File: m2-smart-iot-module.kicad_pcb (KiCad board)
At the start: 4 copper layers, 80.2 x 22.1 mm, 165 parts, among them J1 MM8130-2600RA2, J2 2X05, J3 M.2-M+B-Pins, Q1 BSS123, SW1 PTS840_GK_SMTR_LFS, SW2 PTS840_GK_SMTR_LFS, U1 UPD720202, U10 MIC2877-5.0YFT-TR, U2 SST25VF512A, U3 CoralAccelerator, U4 NRF52840, U5 AP2120N-1.8TRG1, U6 AP22652W6-7, U7 TLV803EF29DBZR, U8 BME280, U9 NCP1599MNTWG, Y1 NX3225SA-24M, Y2 ABM11W-101-32.0000MHZ-T3, Y3 ABS06-32.768KHZ-9-1-T

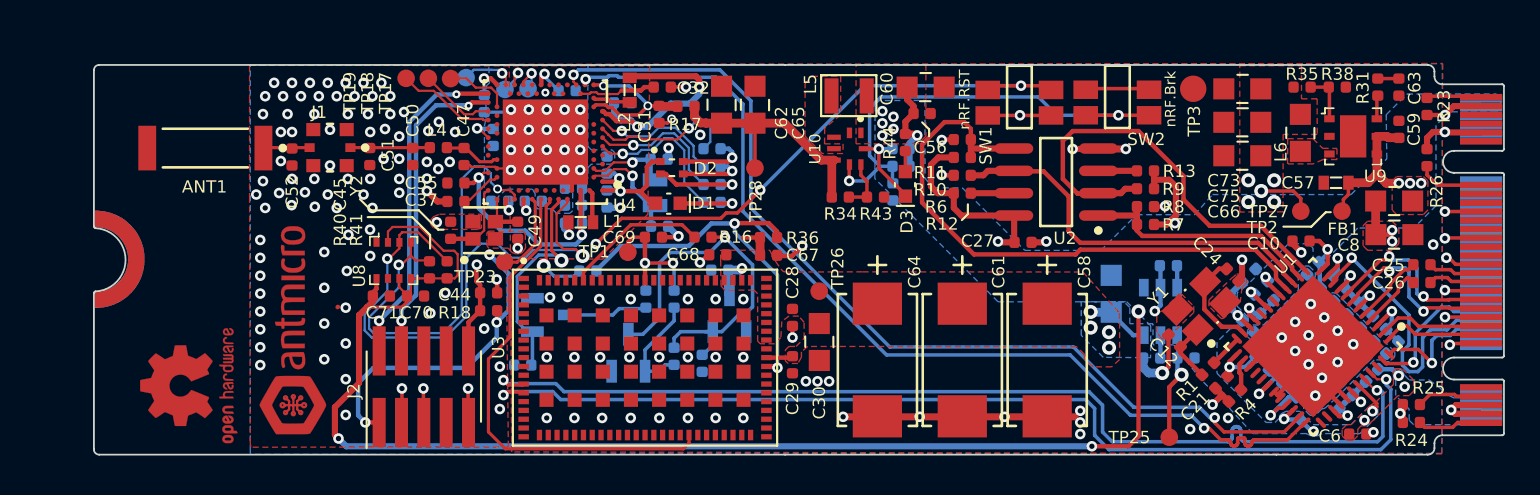
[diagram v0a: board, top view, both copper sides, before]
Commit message: Rearrangement of JTAG connector and U8 sensor
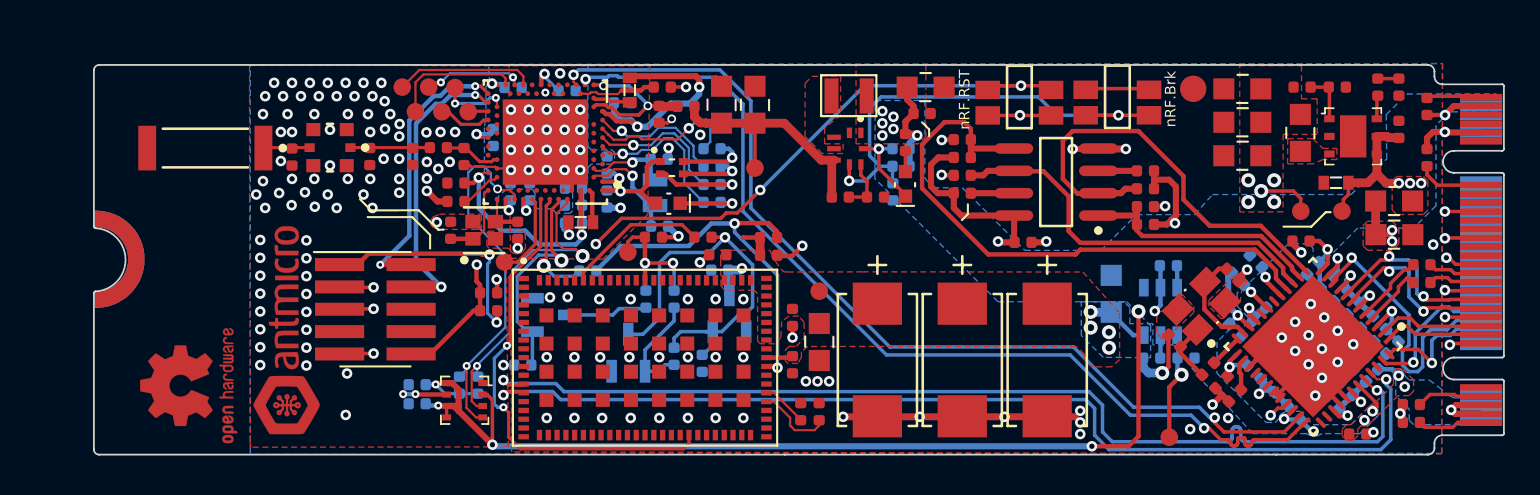
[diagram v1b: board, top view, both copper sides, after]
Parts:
- added R45: R_0R_0402, antmicro-footprints:0402-res, F.Cu at (155.9, 111.2)
- added R46: R_0R_0402, antmicro-footprints:0402-res, F.Cu at (154.9, 111.2)
- C70, C71, R40, R41: moved to B.Cu
- TP11, TP12, TP16: moved to F.Cu
- moved U8 8.91 mm to (135.8, 110.5), turned to 270 degrees
- moved TP11 7.15 mm to (132.2, 92.8)
- moved R41 6.78 mm to (136.6, 109.6)
- moved R40 6.77 mm to (135.5, 109.6)
- moved C70 6.13 mm to (133.1, 110.7), turned to 0 degrees
- moved C71 5.43 mm to (133.1, 109.6), turned to 180 degrees
- moved J2 4.84 mm to (131.0, 105.3), turned to 270 degrees
- moved TP12 4.34 mm to (133.8, 92.8)
- moved TP16 3.53 mm to (133.0, 94.2)
- moved TP18 2.96 mm to (136.0, 94.2)
- moved TP19 2.78 mm to (134.5, 94.2)
- moved C41 1.88 mm to (138.6, 92.7), turned to 0 degrees
- moved R5 0.84 mm to (180.8, 102.6)
- moved C39 0.81 mm to (138.4, 98.7), turned to 90 degrees
- moved R3 0.80 mm to (179.8, 103.6)
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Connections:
- net Net-(C54-Pad1) renamed /CoralAccelerator/1V8_CORAL
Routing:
- net 3V3: track 123.5 -> 106.1 mm, vias 22 -> 24
- net /nRF52840/SDA: track 31.6 -> 18.9 mm
- net Net-(TP11-Pad1): track 1.80 -> 7.93 mm, vias 1 -> 0
- net /nRF52840/VDD: track 47.5 -> 42.6 mm, vias 9 -> 8
- net Net-(R45-Pad1): track 0.00 -> 4.34 mm
- net /nRF52840/SCL: track 25.2 -> 21.1 mm
- net Net-(TP12-Pad1): track 2.18 -> 5.68 mm, vias 1 -> 2
- net Net-(TP18-Pad1): track 4.32 -> 1.17 mm
- net /nRF52840/SWDIO: track 18.9 -> 16.1 mm
- net Net-(R46-Pad1): track 0.00 -> 2.62 mm
- net Net-(TP19-Pad1): track 5.65 -> 3.08 mm
- net Net-(TP16-Pad1): track 4.98 -> 7.35 mm, vias 1 -> 0
- net /nRF52840/~RESET: track 58.2 -> 60.4 mm
- net /nRF52840/SWCLK: track 17.8 -> 16.5 mm
- net GND: track 88.3 -> 89.5 mm, vias 189 -> 185
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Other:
- board text added: "PCIe radio module rev 1.1.0 03/2022"
- board text removed: "ePCI radio module rev 1.1.0 03/2022"

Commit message: Moved antenna out of GND plane
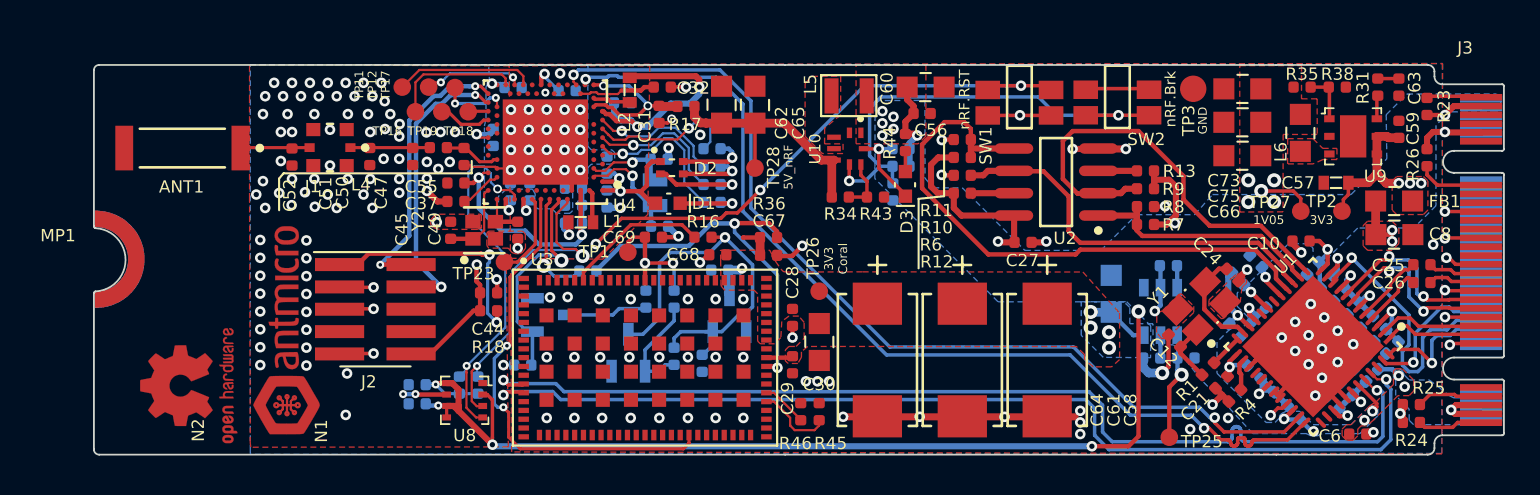
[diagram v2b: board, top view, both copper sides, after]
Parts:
- moved ANT1 1.31 mm to (119.8, 96.2)
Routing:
- net Net-(ANT1-Pad1): track 2.70 -> 3.94 mm
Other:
- board text added: "1V05"
- board text added: "3V3"
- board text added: "3V3 Coral"
- board text added: "5V_nRF"
- board text added: "GND"

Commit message: Updated width and gap of USB and PCIe lanes to correct impedance
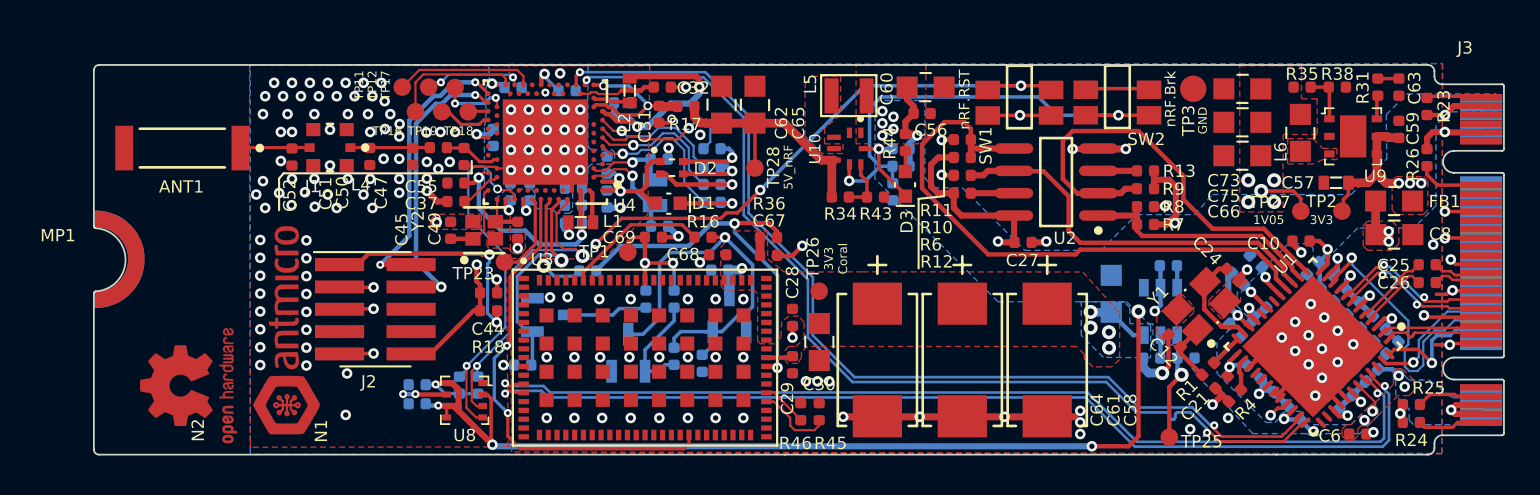
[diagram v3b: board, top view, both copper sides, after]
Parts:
- moved C25 0.30 mm to (190.5, 102.8)
- moved C26 0.30 mm to (190.5, 103.8)
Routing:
- net CORAL_USB_P: track 59.2 -> 56.6 mm
- net GND: track 89.5 -> 91.9 mm
- net PETX_N: track 11.6 -> 9.44 mm
- net PETX_P: track 11.4 -> 9.40 mm
- net CORAL_USB_N: track 58.8 -> 57.3 mm
- net Radio_USB_P: track 54.6 -> 56.1 mm
- net Radio_USB_N: track 55.1 -> 56.1 mm
- net 3V3_CORAL: track 9.35 -> 8.38 mm
- net /PCIe-USB-Bridge/AVDD: track 26.2 -> 25.3 mm
- net 1V05: track 83.6 -> 83.0 mm
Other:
- net class Diff_100 added: clearance 0.125, trace_width 0.25, via_dia 0.46, via_drill 0.2
- net class Diff_90: clearance 0.127 -> 0.125; trace_width 0.28 -> 0.25; via_dia 0.6 -> 0.46; via_drill 0.3 -> 0.2

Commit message: Added stackup table to PCB
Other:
- board text added: "0.018 mm"
- board text added: "0.02 mm"
- board text added: "0.035 mm"
- board text added: "0.12 mm"
- board text added: "0.51 mm"
- board text added: "1"
- board text added: "2"
- board text added: "3"
- board text added: "3.5"
- board text added: "4"
- board text added: "4.2"
- board text added: "5"
- board text added: "6"
- board text added: "7"
- board text added: "8"
- board text added: "9"
- board text added: "Bottom Layer"
- board text added: "Bottom Solder"
- board text added: "Constant"
- board text added: "Copper"
- board text added: "Dielectric 1"
- board text added: "Dielectric 2"
- board text added: "Dielectric 3"
- board text added: "FR-4"
- board text added: "Gold plating (ENIG, selective)"
- board text added: "Layer"
- board text added: "Material"
- board text added: "Name"
- board text added: "Power Plane 1"
- board text added: "Power Plane 2"
- board text added: "Prepreg"
- board text added: "Recommended PCB finish:"
- board text added: "Recommended PCB stackup"
- board text added: "Silkscreen: white"
- board text added: "Solder Resist"
- board text added: "Solder mask: matt black"
- board text added: "Suggested prepreg material is ISOLA PR2116"
- board text added: "The design includes high speed signaling"
- board text added: "Thickness"
- board text added: "Top Layer"
- board text added: "Top Solder"

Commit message: Added 3d models of BME280 and 1V05 DCDC
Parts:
- R45, R46: footprint antmicro-footprints:0402-res -> m2-smart-iot-module-footprints:0402-res
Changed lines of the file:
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@@
     (add_net Radio_USB_P)
+  )
+  (module m2-smart-iot-module-footprints:Pressure_Sensor_LGA-8_2.5x2.5mm_BME280 (layer F.Cu)
+    (at 135.7975 110.5 270)
+    (attr smd)
+    (fp_text reference U8 (at 2 -0.0025) (layer F.SilkS)
+      (effects (font (size 0.7 0.7) (thickness 0.15)))
+    )
+    (fp_text value BME280 (at 0 2.47 90) (layer F.Fab) hide
+      (effects (font (size 1 1) (thickness 0.15)))
+    )
+    (fp_line (start 1.5 1.5) (end -1.5 1.5) (layer F.CrtYd) (width 0.05))
+    (fp_line (start -1.5 -1.5) (end -1.5 1.5) (layer F.CrtYd) (width 0.05))
+    (fp_line (start 1.5 -1.5) (end -1.5 -1.5) (layer F.CrtYd) (width 0.05))
+    (fp_line (start 1.5 -1.5) (end 1.5 1.5) (layer F.CrtYd) (width 0.05))
+    (fp_line (start 1.35 1.35) (end 1.35 0.85) (layer F.SilkS) (width 0.1))
+    (fp_line (start 1.35 1.35) (end 0.85 1.35) (layer F.SilkS) (width 0.1))
+    (fp_line (start -1.35 1.35) (end -1.35 0.85) (layer F.SilkS) (width 0.1))
+    (fp_line (start -1.35 1.35) (end -0.85 1.35) (layer F.SilkS) (width 0.1))
+    (fp_line (start -0.85 -1.35) (end -0.85 -1.55) (layer F.SilkS) (width 0.1))
+    (fp_line (start -1.35 -1.35) (end -1.35 -0.85) (layer F.SilkS) (width 0.1))
+    (fp_line (start -1.35 -1.35) (end -0.85 -1.35) (layer F.SilkS) (width 0.1))
+    (fp_line (start 1.35 -1.35) (end 1.35 -0.975) (layer F.SilkS) (width 0.1))
+    (fp_line (start 1.35 -1.35) (end 0.975 -1.35) (layer F.SilkS) (width 0.1))
+    (fp_text user %R (at 0 0 90) (layer F.Fab)
+      (effects (font (size 0.7 0.7) (thickness 0.05)))
+    )
+    (fp_line (start 1.25 -1.25) (end 1.25 1.25) (layer F.Fab) (width 0.1))
+    (fp_line (start 1.25 1.25) (end -1.25 1.25) (layer F.Fab) (width 0.1))
+    (fp_line (start -1.25 1.25) (end -1.25 -1.25) (layer F.Fab) (width 0.1))
+    (fp_line (start -1.25 -1.25) (end 1.25 -1.25) (layer F.Fab) (width 0.1))
+    (pad 1 smd rect (at -0.975 -1.025 270) (size 0.35 0.5) (layers F.Cu F.Paste F.Mask)
+      (net 1 GND))
+    (pad 2 smd rect (at -0.325 -1.025 270) (size 0.35 0.5) (layers F.Cu F.Paste F.Mask)
+      (net 2 3V3))
+    (pad 3 smd rect (at 0.325 -1.025 270) (size 0.35 0.5) (layers F.Cu F.Paste F.Mask)
+      (net 146 /nRF52840/SDA))
+    (pad 4 smd rect (at 0.975 -1.025 270) (size 0.35 0.5) (layers F.Cu F.Paste F.Mask)
+      (net 147 /nRF52840/SCL))
+    (pad 5 smd rect (at 0.975 1.024999 270) (size 0.35 0.5) (layers F.Cu F.Paste F.Mask)
+      (net 2 3V3))
+    (pad 6 smd rect (at 0.325 1.024999 270) (size 0.35 0.5) (layers F.Cu F.Paste F.Mask)
+      (net 2 3V3))
+    (pad 7 smd rect (at -0.325 1.024999 270) (size 0.35 0.5) (layers F.Cu F.Paste F.Mask)
+      (net 1 GND))
+    (pad 8 smd rect (at -0.975 1.024999 270) (size 0.35 0.5) (layers F.Cu F.Paste F.Mask)
+      (net 2 3V3))
+    (model ${KIPRJMOD}/lib/3d-models/BME280.STEP
+      (at (xyz 0 0 0))
+      (scale (xyz 1 1 1))
+      (rotate (xyz -90 0 180))
+    )
   )
   (module m2-smart-iot-module-footprints:ARM_SWD (layer F.Cu)
@@
     )
   )
-  (module antmicro-footprints:0402-res (layer F.Cu)
+  (module m2-smart-iot-module-footprints:0402-res (layer F.Cu)
     (at 154.9 111.15 90)
     (descr "Resistor SMD 0402 (1005 Metric), square (rectangular) end terminal, IPC_7351 nominal, (Body size source: http://www.tortai-tech.com/upload/download/2011102023233369053.pdf), generated with kicad-footprint-generator")
@@
     (pad 1 smd roundrect (at -0.485 0 90) (size 0.59 0.64) (layers F.Cu F.Paste F.Mask) (roundrect_rratio 0.25)
       (net 178 "Net-(R46-Pad1)"))
-    (model ${ANT3DMDL}/0402-res.step
+    (model ${KIPRJMOD}/lib/3d-models/0402-res.step
       (offset (xyz 0 0 -0.01))
       (scale (xyz 1 1 1))
@@
     )
   )
-  (module antmicro-footprints:0402-res (layer F.Cu)
+  (module m2-smart-iot-module-footprints:0402-res (layer F.Cu)
     (at 155.95 111.15 90)
     (descr "Resistor SMD 0402 (1005 Metric), square (rectangular) end terminal, IPC_7351 nominal, (Body size source: http://www.tortai-tech.com/upload/download/2011102023233369053.pdf), generated with kicad-footprint-generator")
@@
     (pad 1 smd roundrect (at -0.485 0 90) (size 0.59 0.64) (layers F.Cu F.Paste F.Mask) (roundrect_rratio 0.25)
       (net 177 "Net-(R45-Pad1)"))
-    (model ${ANT3DMDL}/0402-res.step
+    (model ${KIPRJMOD}/lib/3d-models/0402-res.step
       (offset (xyz 0 0 -0.01))
       (scale (xyz 1 1 1))
@@
     )
   )
-  (module m2-smart-iot-module-footprints:Pressure_Sensor_LGA-8_2.5x2.5mm_BME280 (layer F.Cu)
-    (at 135.7975 110.5 270)
-    (attr smd)
-    (fp_text reference U8 (at 2 -0.0025) (layer F.SilkS)
-      (effects (font (size 0.7 0.7) (thickness 0.15)))
-    )
-    (fp_text value BME280 (at 0 2.47 90) (layer F.Fab) hide
-      (effects (font (size 1 1) (thickness 0.15)))
-    )
-    (fp_line (start 1.5 1.5) (end -1.5 1.5) (layer F.CrtYd) (width 0.05))
-    (fp_line (start -1.5 -1.5) (end -1.5 1.5) (layer F.CrtYd) (width 0.05))
-    (fp_line (start 1.5 -1.5) (end -1.5 -1.5) (layer F.CrtYd) (width 0.05))
-    (fp_line (start 1.5 -1.5) (end 1.5 1.5) (layer F.CrtYd) (width 0.05))
-    (fp_line (start 1.35 1.35) (end 1.35 0.85) (layer F.SilkS) (width 0.1))
-    (fp_line (start 1.35 1.35) (end 0.85 1.35) (layer F.SilkS) (width 0.1))
-    (fp_line (start -1.35 1.35) (end -1.35 0.85) (layer F.SilkS) (width 0.1))
-    (fp_line (start -1.35 1.35) (end -0.85 1.35) (layer F.SilkS) (width 0.1))
-    (fp_line (start -0.85 -1.35) (end -0.85 -1.55) (layer F.SilkS) (width 0.1))
-    (fp_line (start -1.35 -1.35) (end -1.35 -0.85) (layer F.SilkS) (width 0.1))
-    (fp_line (start -1.35 -1.35) (end -0.85 -1.35) (layer F.SilkS) (width 0.1))
-    (fp_line (start 1.35 -1.35) (end 1.35 -0.975) (layer F.SilkS) (width 0.1))
-    (fp_line (start 1.35 -1.35) (end 0.975 -1.35) (layer F.SilkS) (width 0.1))
-    (fp_line (start 1.25 -1.25) (end 1.25 1.25) (layer F.Fab) (width 0.1))
-    (fp_line (start 1.25 1.25) (end -1.25 1.25) (layer F.Fab) (width 0.1))
-    (fp_line (start -1.25 1.25) (end -1.25 -1.25) (layer F.Fab) (width 0.1))
-    (fp_line (start -1.25 -1.25) (end 1.25 -1.25) (layer F.Fab) (width 0.1))
-    (fp_text user %R (at 0 0 90) (layer F.Fab)
-      (effects (font (size 0.7 0.7) (thickness 0.05)))
-    )
-    (pad 8 smd rect (at -0.975 1.024999 270) (size 0.35 0.5) (layers F.Cu F.Paste F.Mask)
-      (net 2 3V3))
-    (pad 7 smd rect (at -0.325 1.024999 270) (size 0.35 0.5) (layers F.Cu F.Paste F.Mask)
-      (net 1 GND))
-    (pad 6 smd rect (at 0.325 1.024999 270) (size 0.35 0.5) (layers F.Cu F.Paste F.Mask)
-      (net 2 3V3))
-    (pad 5 smd rect (at 0.975 1.024999 270) (size 0.35 0.5) (layers F.Cu F.Paste F.Mask)
-      (net 2 3V3))
-    (pad 4 smd rect (at 0.975 -1.025 270) (size 0.35 0.5) (layers F.Cu F.Paste F.Mask)
-      (net 147 /nRF52840/SCL))
-    (pad 3 smd rect (at 0.325 -1.025 270) (size 0.35 0.5) (layers F.Cu F.Paste F.Mask)
-      (net 146 /nRF52840/SDA))
-    (pad 2 smd rect (at -0.325 -1.025 270) (size 0.35 0.5) (layers F.Cu F.Paste F.Mask)
-      (net 2 3V3))
-    (pad 1 smd rect (at -0.975 -1.025 270) (size 0.35 0.5) (layers F.Cu F.Paste F.Mask)
-      (net 1 GND))
-  )
   (module m2-smart-iot-module-footprints:Nordic_Semiconductor-NRF52840-QIAA-R-0-0-MFG (layer F.Cu)

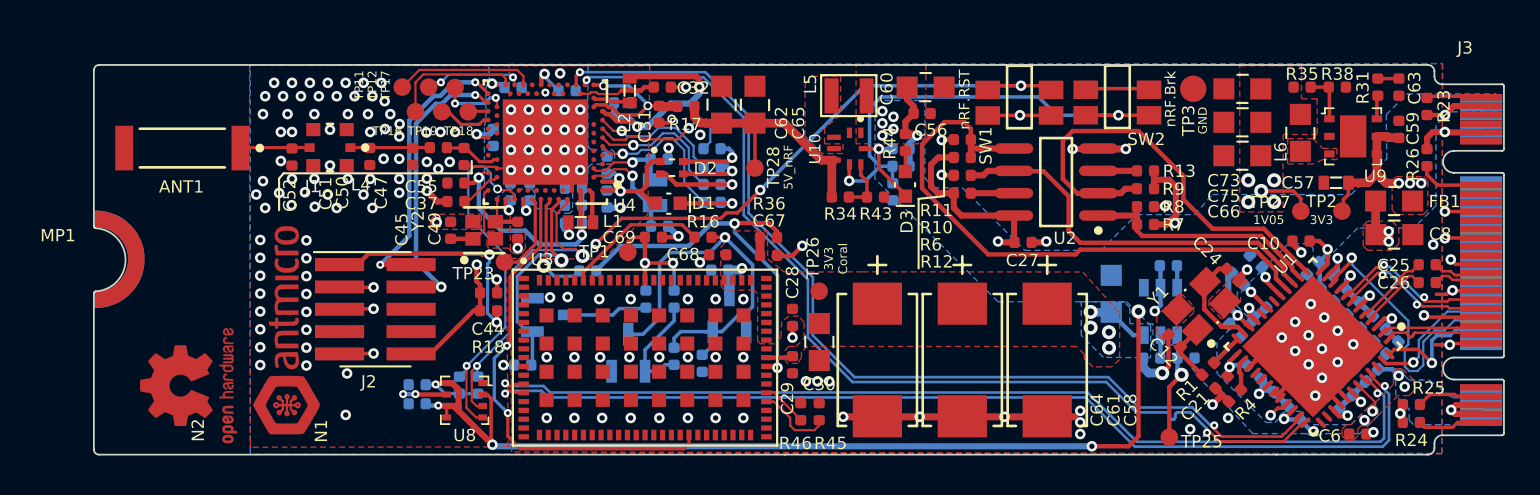
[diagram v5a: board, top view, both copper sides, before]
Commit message: Silkscreen improvements, removed DRC errors on M.2 connector
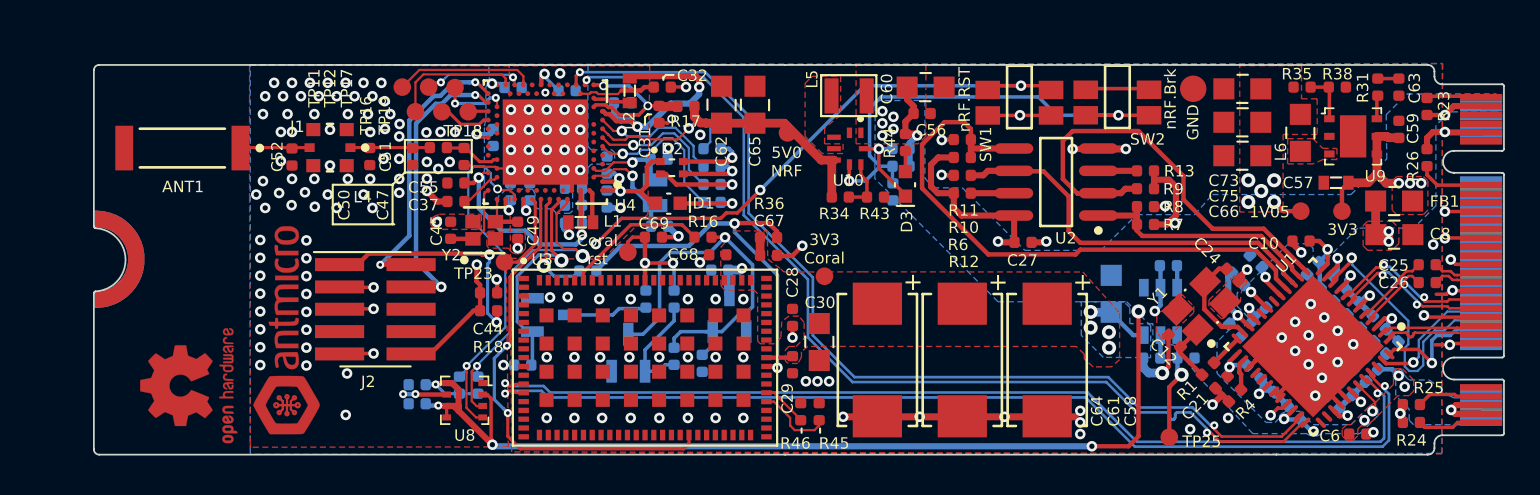
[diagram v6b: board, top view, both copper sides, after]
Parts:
- moved TP28 2.72 mm to (154.2, 95.3)
- moved TP26 0.90 mm to (156.3, 103.5)
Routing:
- net 5V_RADIO: track 14.2 -> 12.1 mm
- net 1V05: track 83.0 -> 81.5 mm
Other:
- board text added: "5V0 NRF"
- board text added: "Coral rst"
- board text removed: "5V_nRF"
